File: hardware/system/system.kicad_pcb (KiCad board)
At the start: 2 copper layers, 226.6 x 87.2 mm, 45 parts, among them J1 CART_SOCKET_28P, J2 EXTENSION PINS, SW1 POWER, SW2 RESET, SW3 A, SW4 B, SW5 UP, SW6 DN, SW7 LF, SW8 RT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

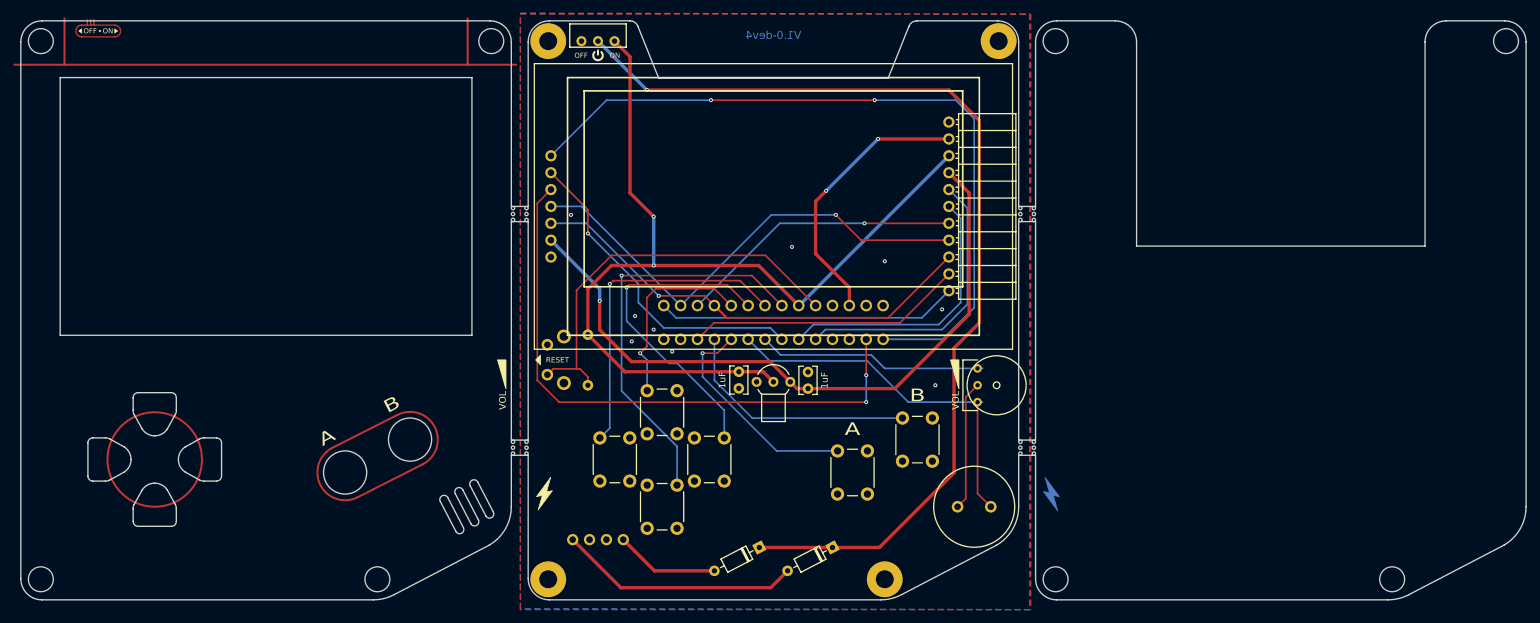
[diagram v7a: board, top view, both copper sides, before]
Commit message: Finish 1.0-dev4 updates
- Add stylistic display cutout
- Add support under charger board
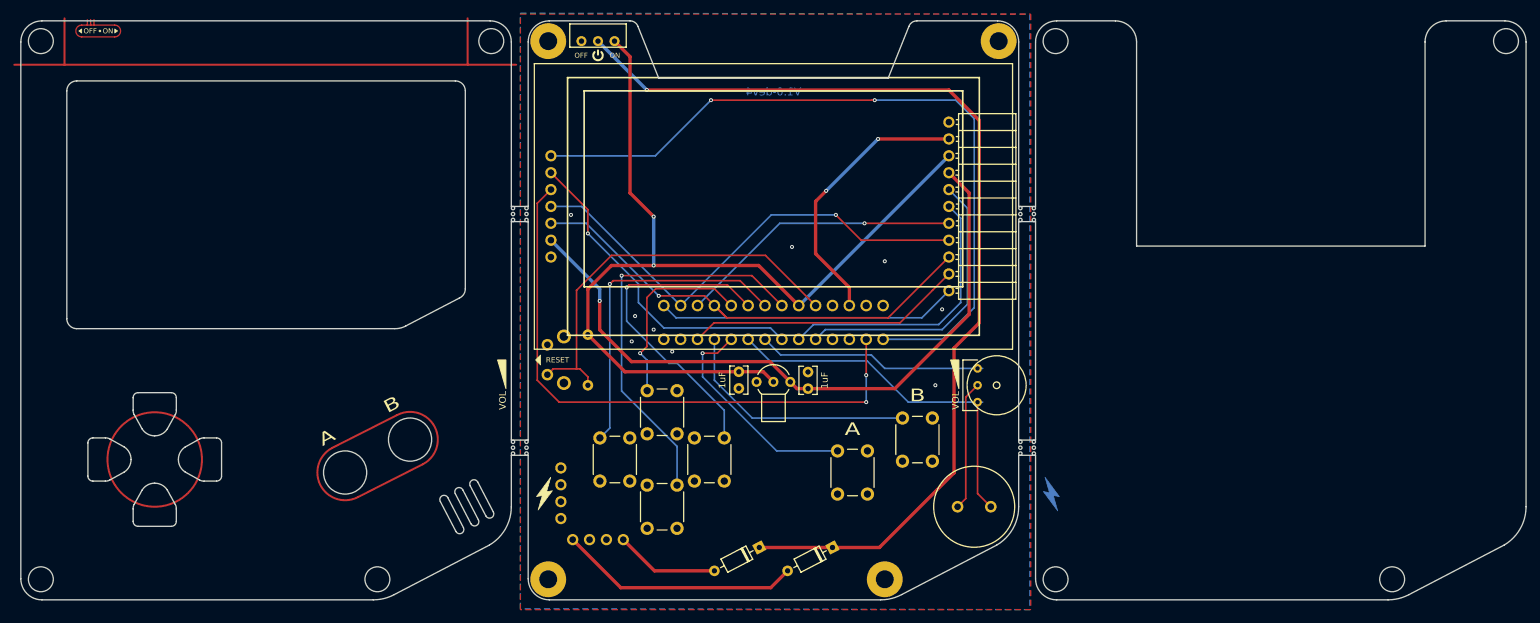
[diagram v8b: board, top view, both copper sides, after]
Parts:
- added **REF: SUPPORT, system:01X04_HEADER, B.Cu at (107.7, 138.2)
